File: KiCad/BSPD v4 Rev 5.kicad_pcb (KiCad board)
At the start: 4 copper layers, 100 x 77.5 mm, 197 parts, among them J1 DTM13-12PA, U1 LM339, U10 2N7002, U11 2N7002, U12 2N7002, U13 2N7002, U14 2N7002, U15 2N7002, U16 2N7002, U17 74HC08D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

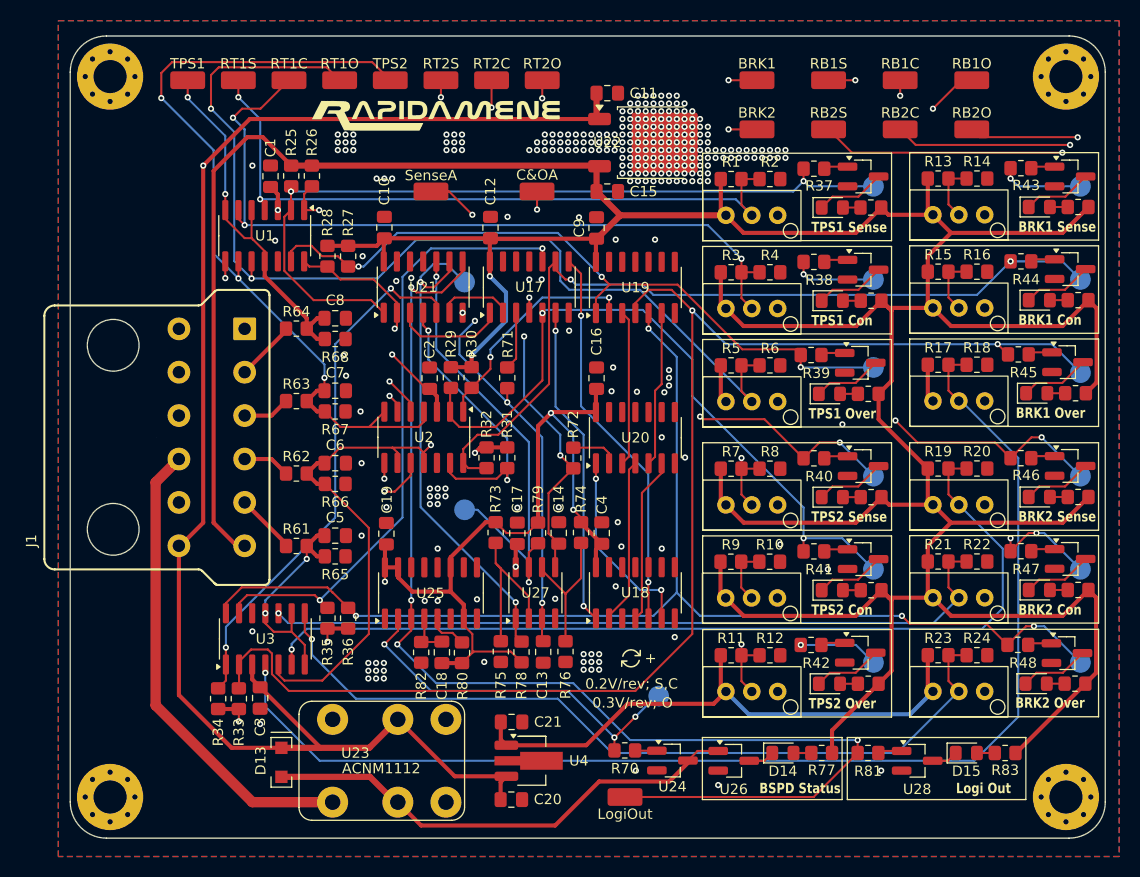
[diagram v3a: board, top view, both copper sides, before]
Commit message: Added support for differential input, Changed LED colors and resistor
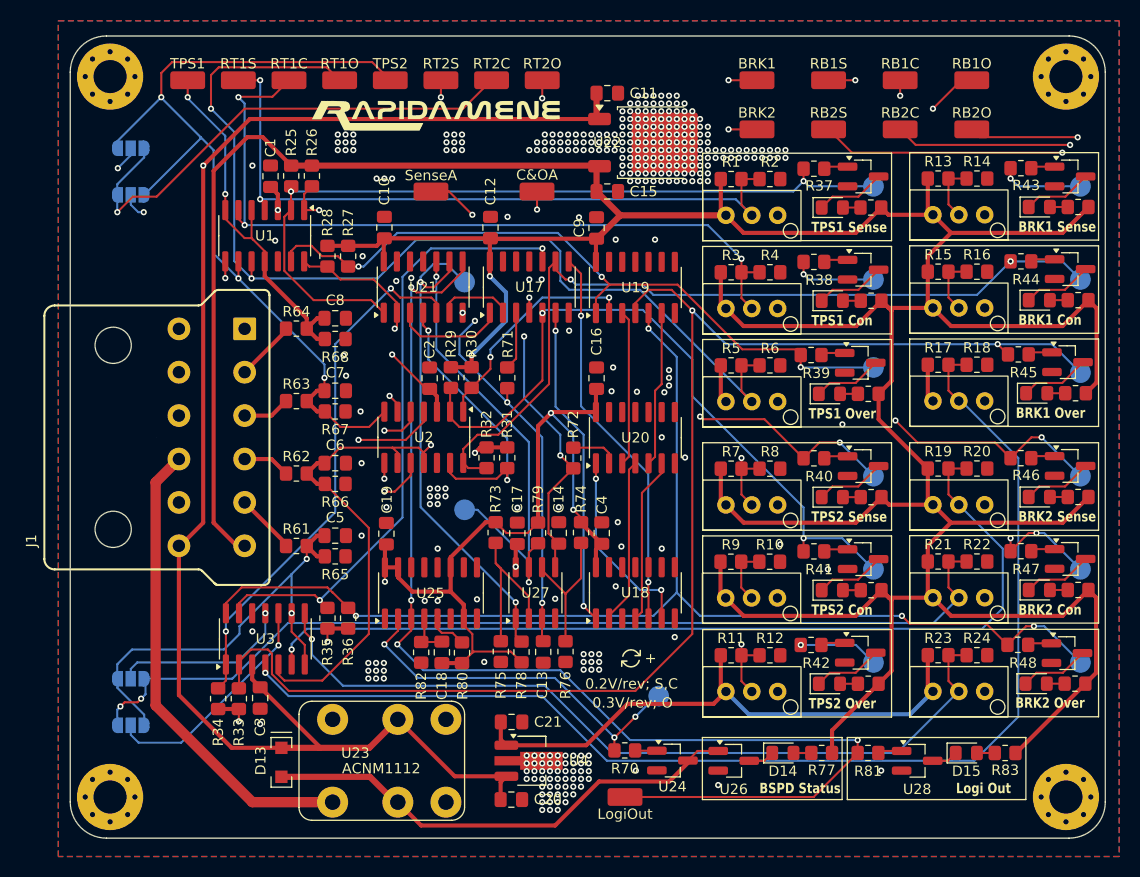
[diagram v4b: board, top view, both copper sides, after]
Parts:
- added JP1: SolderJumper_3_Open, Test Hook:SolderedJumper 3P, B.Cu at (147.0, 78.3)
- added JP2: SolderJumper_3_Open, Test Hook:SolderedJumper 3P, B.Cu at (147.0, 82.8)
- added JP3: SolderJumper_3_Open, Test Hook:SolderedJumper 3P, B.Cu at (147.0, 129.6)
- added JP4: SolderJumper_3_Open, Test Hook:SolderedJumper 3P, B.Cu at (147.0, 134.1)
- D1, D10, D4, D7: value LED -> YLED
- D11, D2, D5, D8: value LED -> GLED
- D12, D14, D15, D3, D6, D9: value LED -> RLED
- R49, R51, R52, R54, R55, R57, R58, R60, R77, R83: value R150 -> R200
- R50, R53, R56, R59: value R150 -> R82
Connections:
- R10 pad 1: Net-(U2A-+) -> Net-(JP1-A)
- R21 pad 2: Net-(U3C--) -> Net-(JP3-A)
- R22 pad 1: Net-(U3C--) -> Net-(JP3-A)
- R9 pad 2: Net-(U2A-+) -> Net-(JP1-A)
- RV11 pad 2: Net-(U3C--) -> Net-(JP3-A)
- RV5 pad 2: Net-(U2A-+) -> Net-(JP1-A)
- TP11 pad 1: Net-(U3C--) -> Net-(JP3-A)
- TP7 pad 1: Net-(U2A-+) -> Net-(JP1-A)
- U2 pad 4: TPS2 -> Net-(JP2-C)
- U2 pad 5: Net-(U2A-+) -> Net-(JP1-C)
- U3 pad 10: Net-(U3C--) -> Net-(JP4-C)
- U3 pad 11: BRK2 -> Net-(JP3-C)
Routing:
- net Net-(JP3-A): track 0.00 -> 165.8 mm, vias 0 -> 3
- net Net-(U3C--): track 144.6 -> 0.00 mm, vias 2 -> 0
- net Net-(JP1-A): track 0.00 -> 131.1 mm, vias 0 -> 1
- net Net-(U2A-+): track 88.5 -> 0.00 mm, vias 2 -> 0
- net Net-(JP1-C): track 0.00 -> 46.6 mm, vias 0 -> 2
- net Net-(JP2-C): track 0.00 -> 44.5 mm, vias 0 -> 2
- net BRK2: track 105.1 -> 128.0 mm
- net Net-(JP4-C): track 0.00 -> 22.5 mm, vias 0 -> 1
- net Net-(JP3-C): track 0.00 -> 17.3 mm, vias 0 -> 1
- net TPS2: track 79.9 -> 88.0 mm
- net Net-(U3A--): track 162.1 -> 160.2 mm
- net Net-(U1A--): track 67.4 -> 68.6 mm
- net GND: vias 278 -> 332

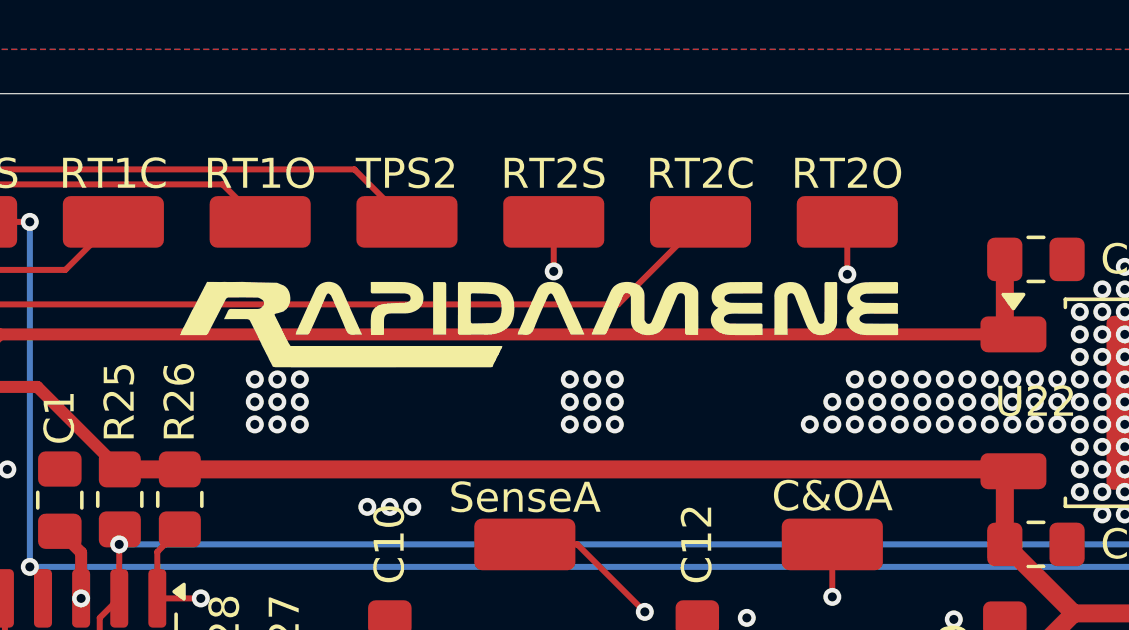
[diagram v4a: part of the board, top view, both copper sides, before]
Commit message: Updated Silkscreen
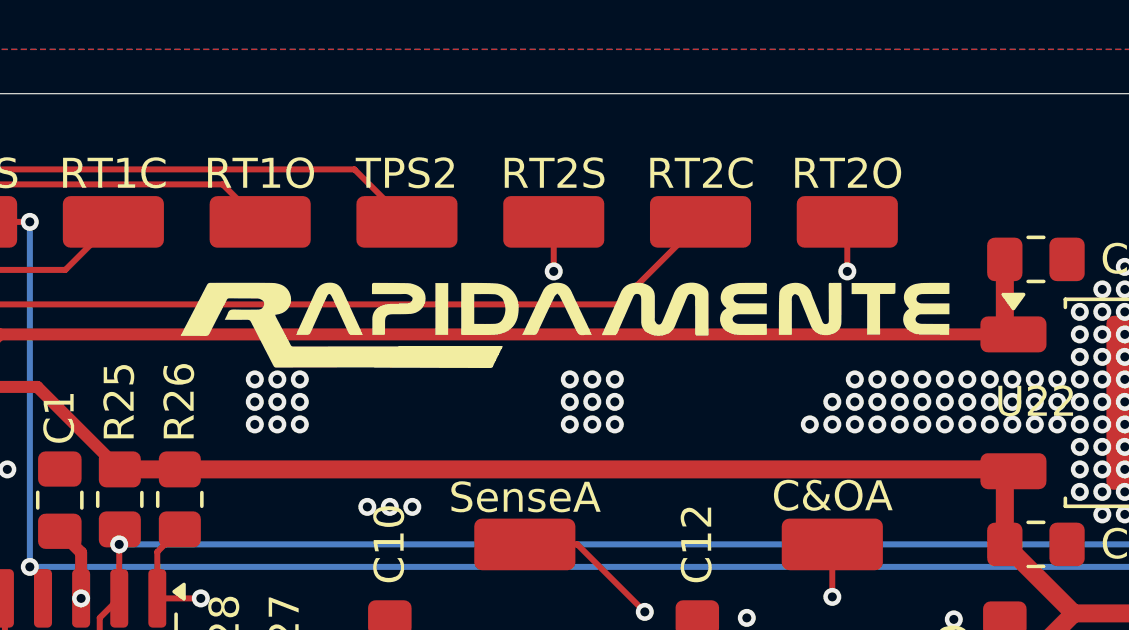
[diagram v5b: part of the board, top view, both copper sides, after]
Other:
- board text added: "Invalid"
